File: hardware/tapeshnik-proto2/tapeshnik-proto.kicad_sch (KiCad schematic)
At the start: 130 parts, among them J1 Conn_01x02, J10 Conn_01x09, J2 RW_HEAD, J3 Conn_01x07, J4 ERASERHEAD, J5 RW_HEAD, J6 Conn_01x01_Pin, J7 Conn_01x01_Pin, J8 Conn_01x01_Pin, J9 Conn_01x01_Pin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

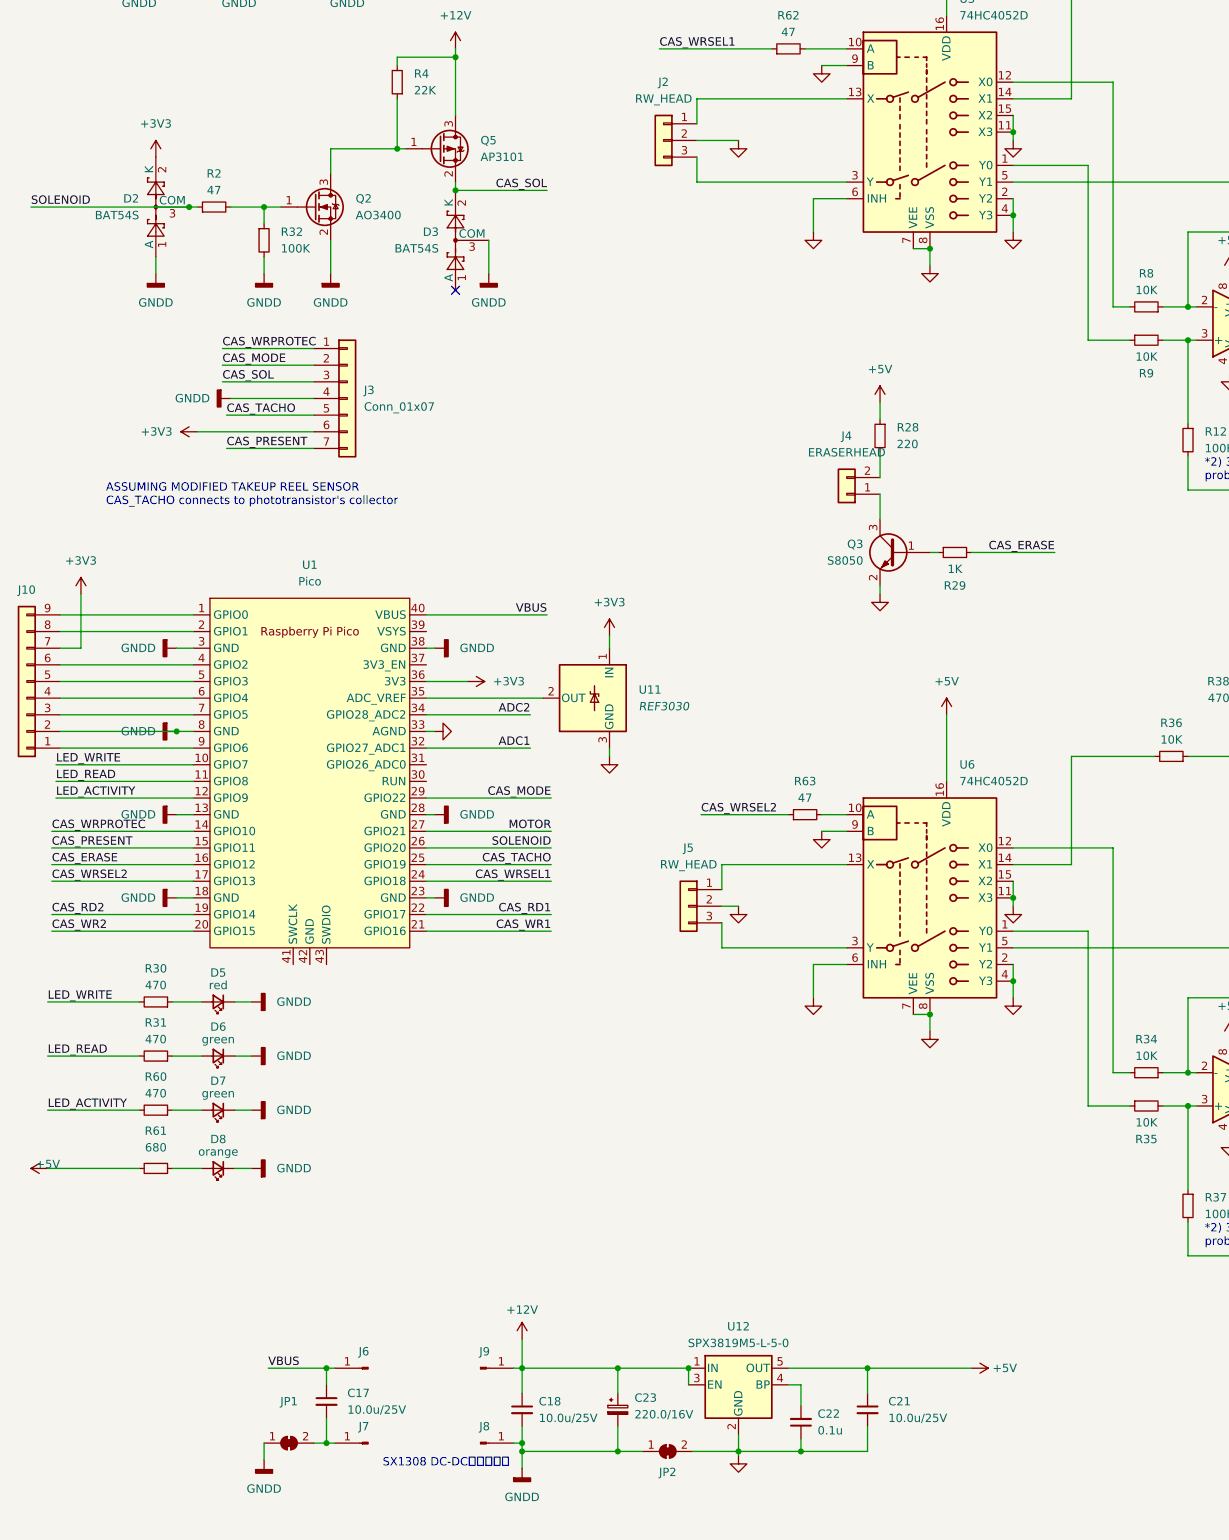
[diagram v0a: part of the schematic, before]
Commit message: updated schematics
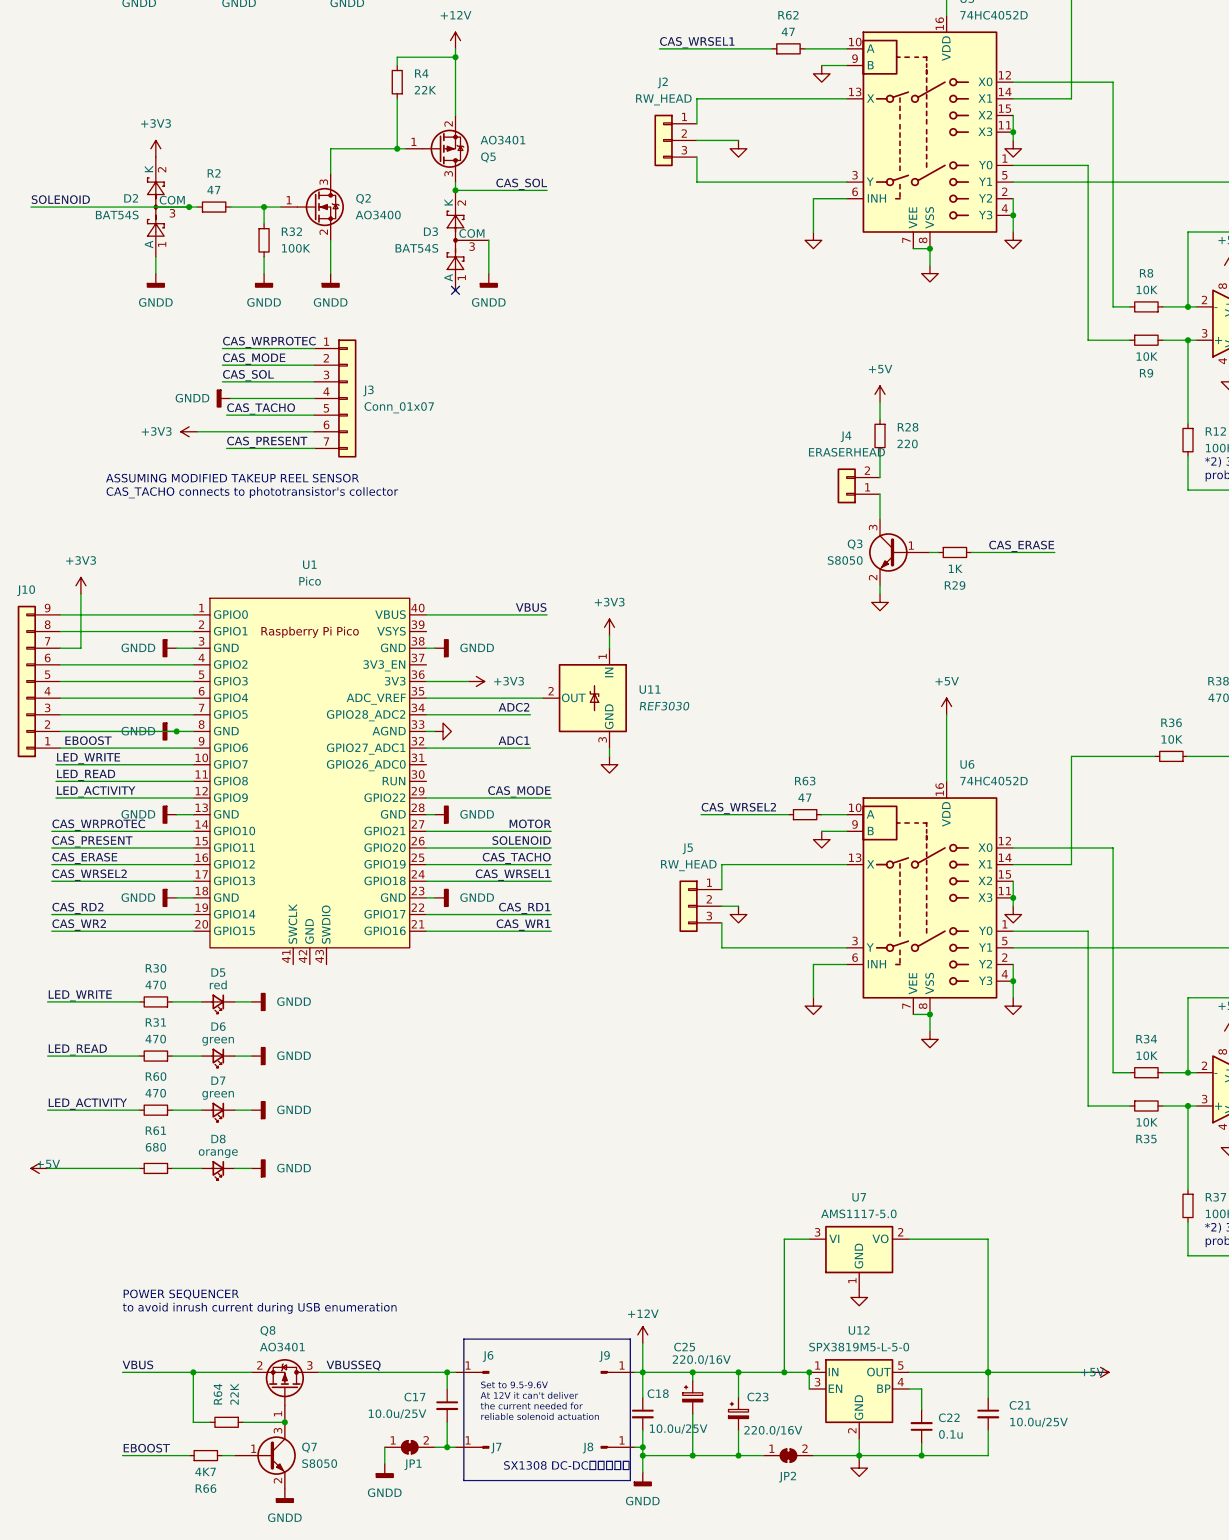
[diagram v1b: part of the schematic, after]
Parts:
- added C25: 220.0/16V, Capacitor_Tantalum_SMD:CP_EIA-7343-31_Kemet-D, symbol Device:C_Polarized_Small
- added Q7: S8050, Package_TO_SOT_SMD:SOT-23, symbol Device:Q_NPN_BEC
- added Q8: AO3401, Package_TO_SOT_SMD:SOT-23, symbol Device:Q_PMOS_GSD
- added R64: 22K, Resistor_SMD:R_0805_2012Metric, symbol Device:R_Small
- added R66: 4K7, Resistor_SMD:R_0805_2012Metric, symbol Device:R_Small
- added U7: AMS1117-5.0, Package_TO_SOT_SMD:SOT-223-3_TabPin2, symbol Regulator_Linear:AMS1117-5.0
- Q5: value AP3101 -> AO3401
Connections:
- net +12V: now also Q5.2 (S), C25.1, U7.3 (VI); no longer Q5.3 (D)
- net +5V: now also U7.2 (VO)
- net CAS_SOL: now also Q5.3 (D); no longer Q5.2 (S)
- net GND: now also U7.1 (GND)
- net GNDD: now also C25.2, Q7.2 (E)
- net VBUS: now also Q8.2 (S), R64.2; no longer C17.1, J6.1 (Pin_1)
- net EBOOST: now reaches J10.1 (Pin_1), U1.9 (GPIO6)
- net EBOOST: now also R66.1
- new net: Q7.3 (C), Q8.1 (G), R64.1
- new net: Q7.1 (B), R66.2
- new net VBUSSEQ: C17.1, J6.1 (Pin_1), Q8.3 (D)
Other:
- note added: "POWER SEQUENCER to avoid inrush current during USB enumeration"
- note added: "Set to 9.5-9.6V At 12V it can't deliver the current needed for reliable solenoid actuation"
- title: (none) -> Tapeshnik proto2
- moved on the sheet: C17, C18, C21, C22, C23, J6, J7, J8, J9, JP1, JP2, U12

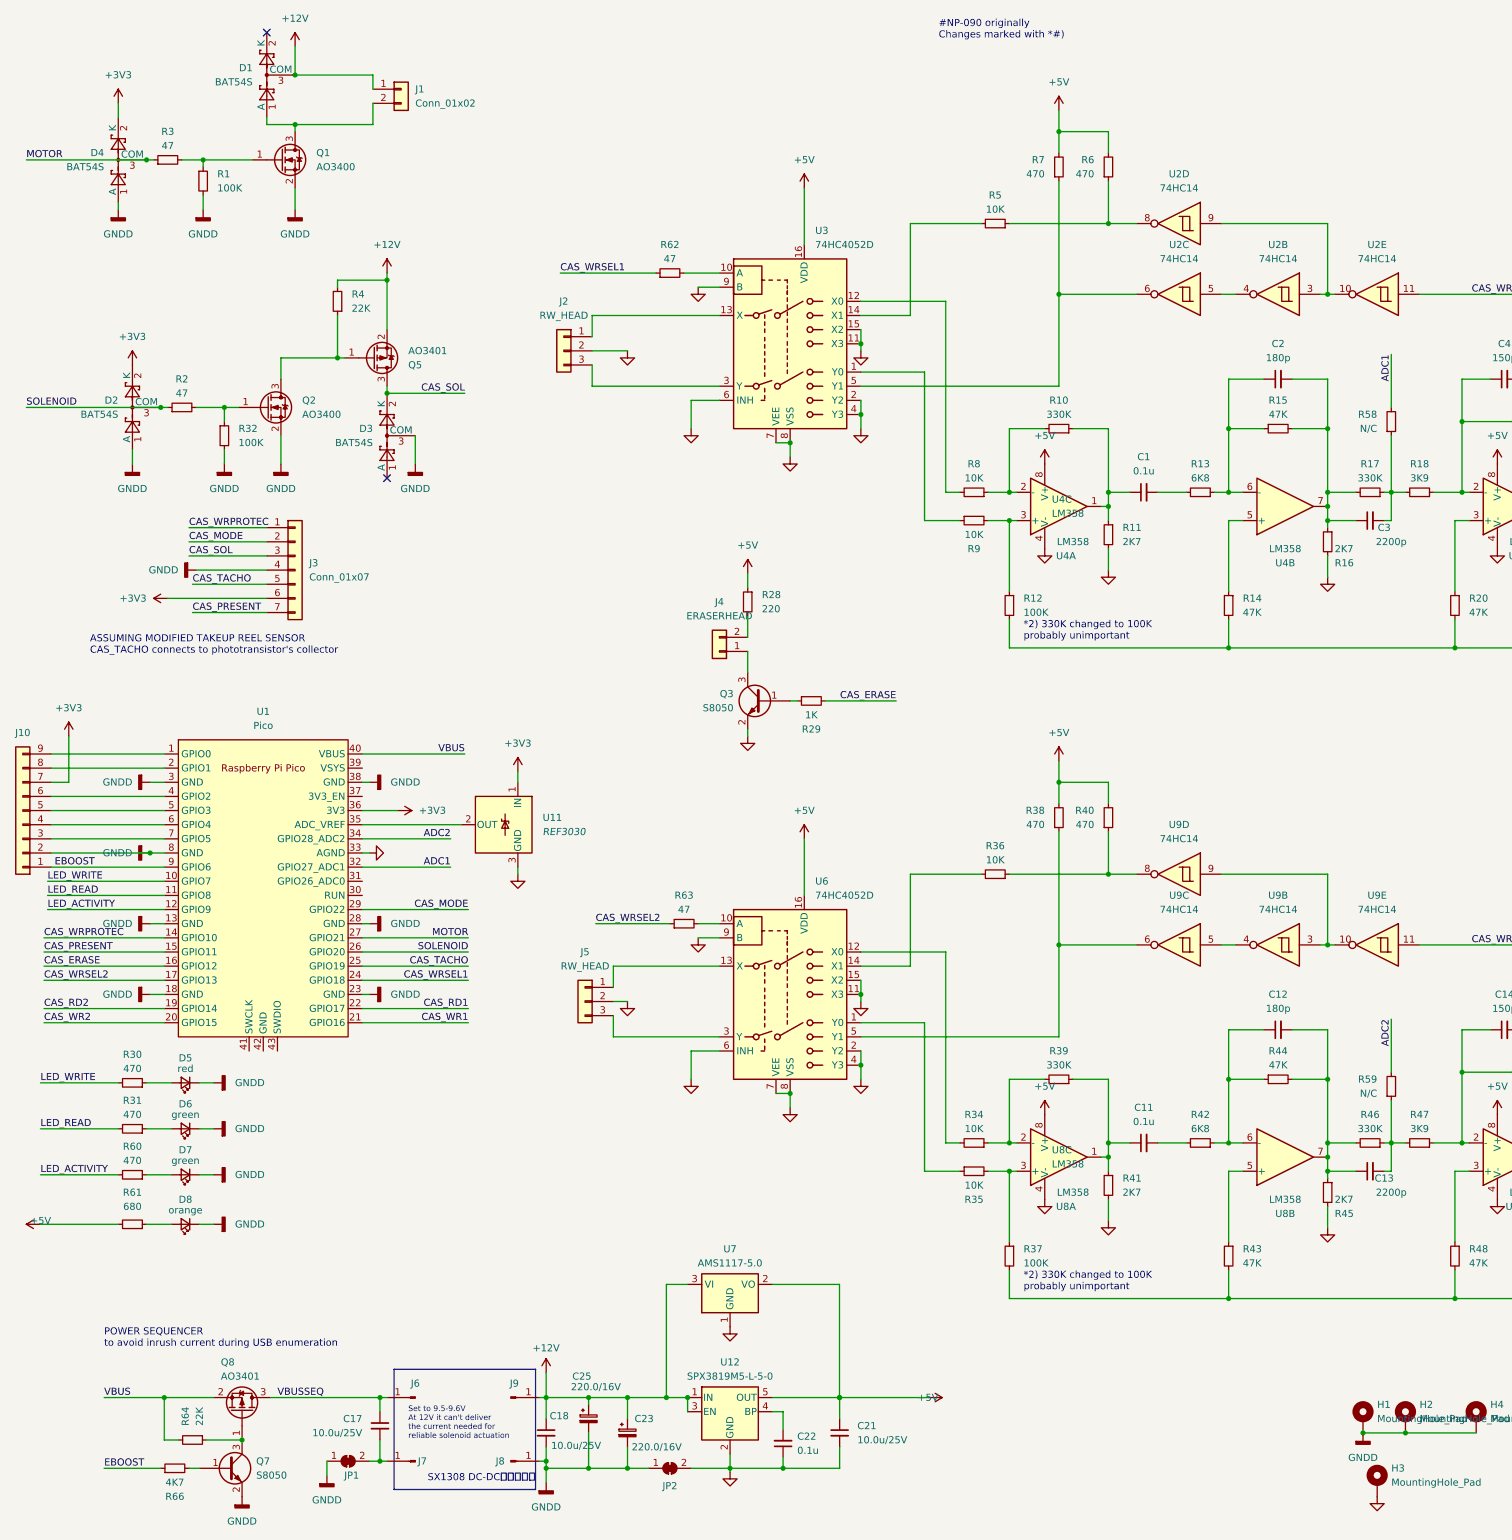
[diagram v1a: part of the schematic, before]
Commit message: updated schematics
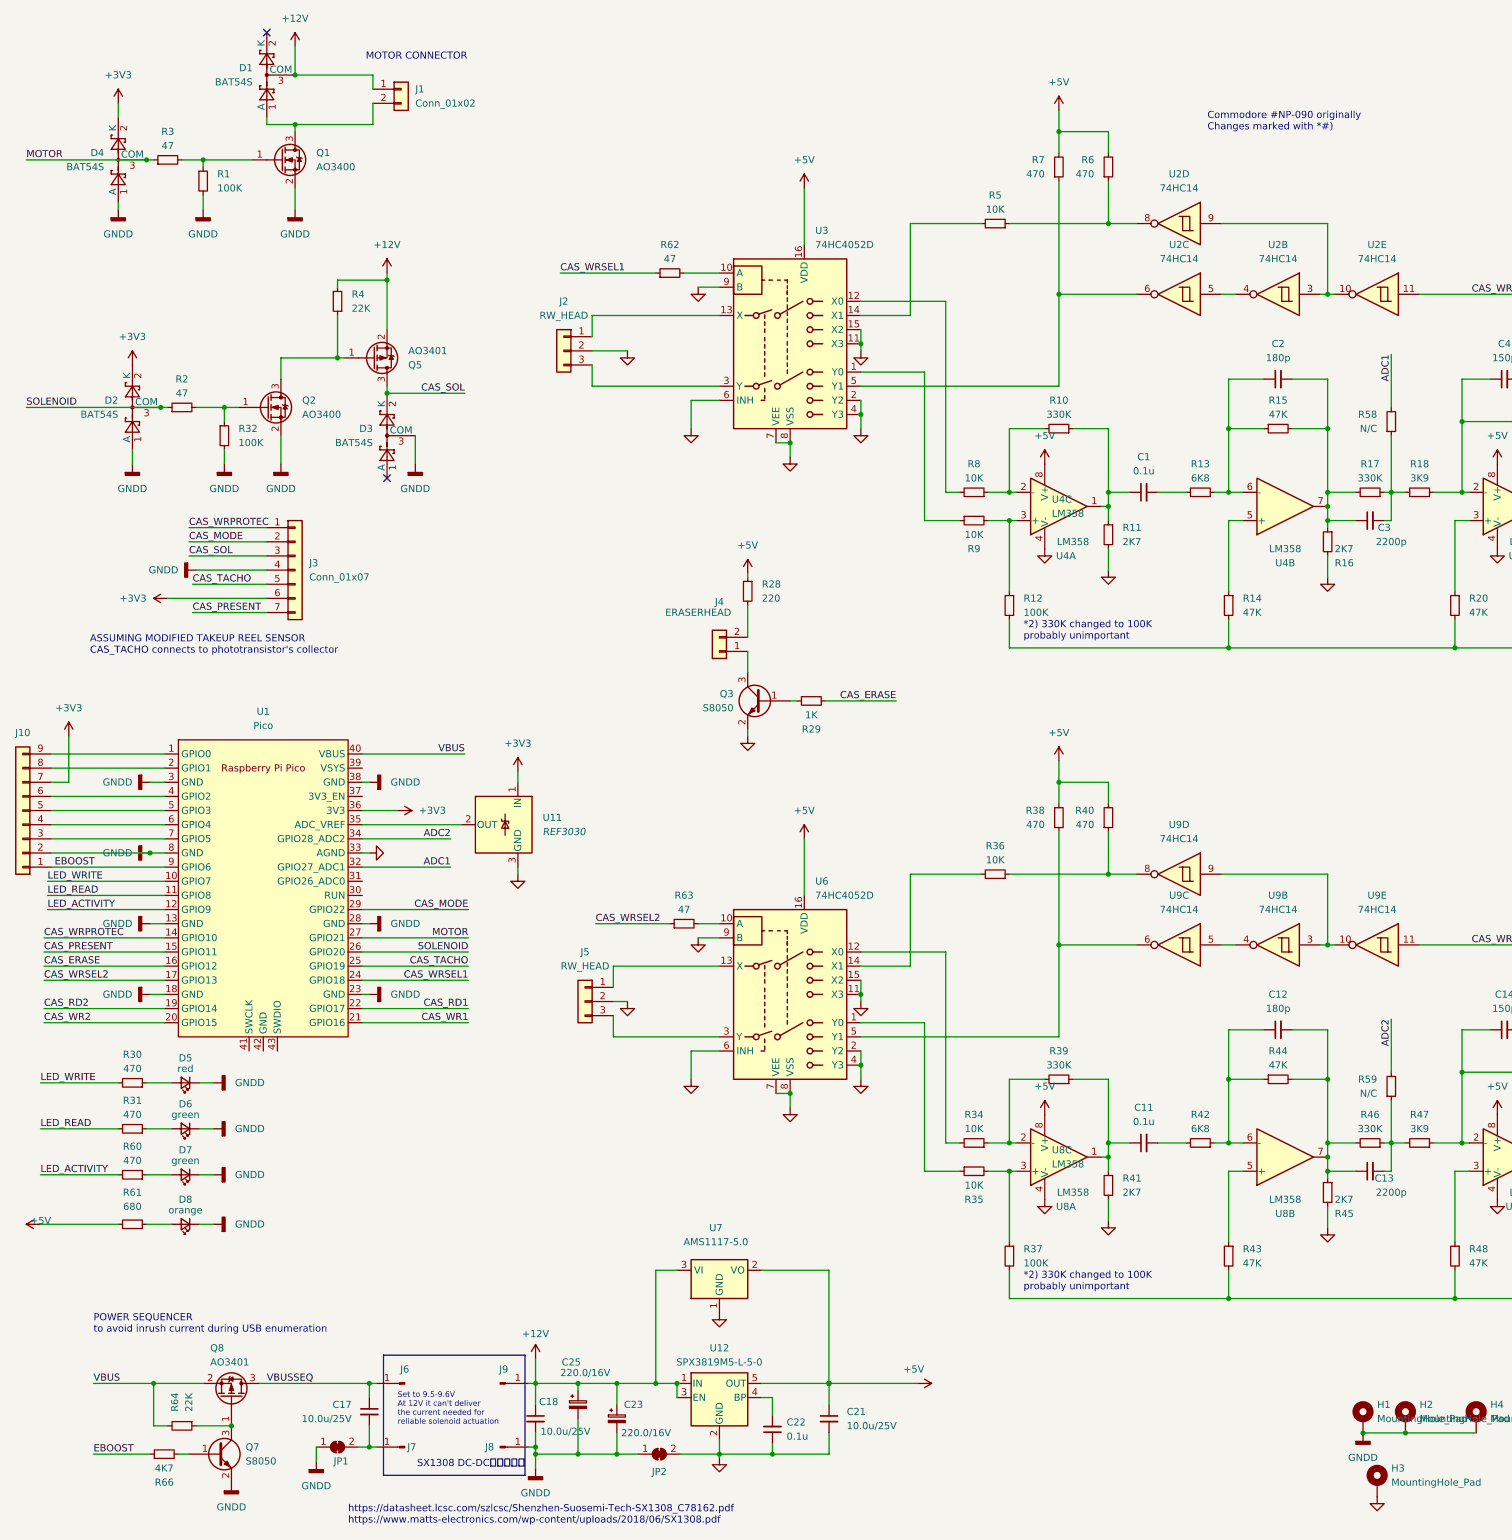
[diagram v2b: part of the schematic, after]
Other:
- note added: "Commodore #NP-090 originally Changes marked with *#)"
- note added: "MOTOR CONNECTOR"
- note added: "https://datasheet.lcsc.com/szlcsc/Shenzhen-Suosemi-Tech-SX1308_C78162.pdf https://www.matts-electronics.com/wp-content/uploads/2018/06/SX1308.pdf"
- note removed: "#NP-090 originally Changes marked with *#)"
- company: (none) -> https://caglrc.cc
- title: Tapeshnik proto2 -> Tapeshnik proto 2
- moved on the sheet: C17, C18, C21, C22, C23, C25, J6, J7, J8, J9, JP1, JP2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
